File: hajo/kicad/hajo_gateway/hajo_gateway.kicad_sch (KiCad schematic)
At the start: 20 parts, among them J1 Seetalk NG, J2 WitMtoion, U1 MCP2562, U2 LF50, U3 WeMos_S2_mini, U4 LF33, U5 MAX3232

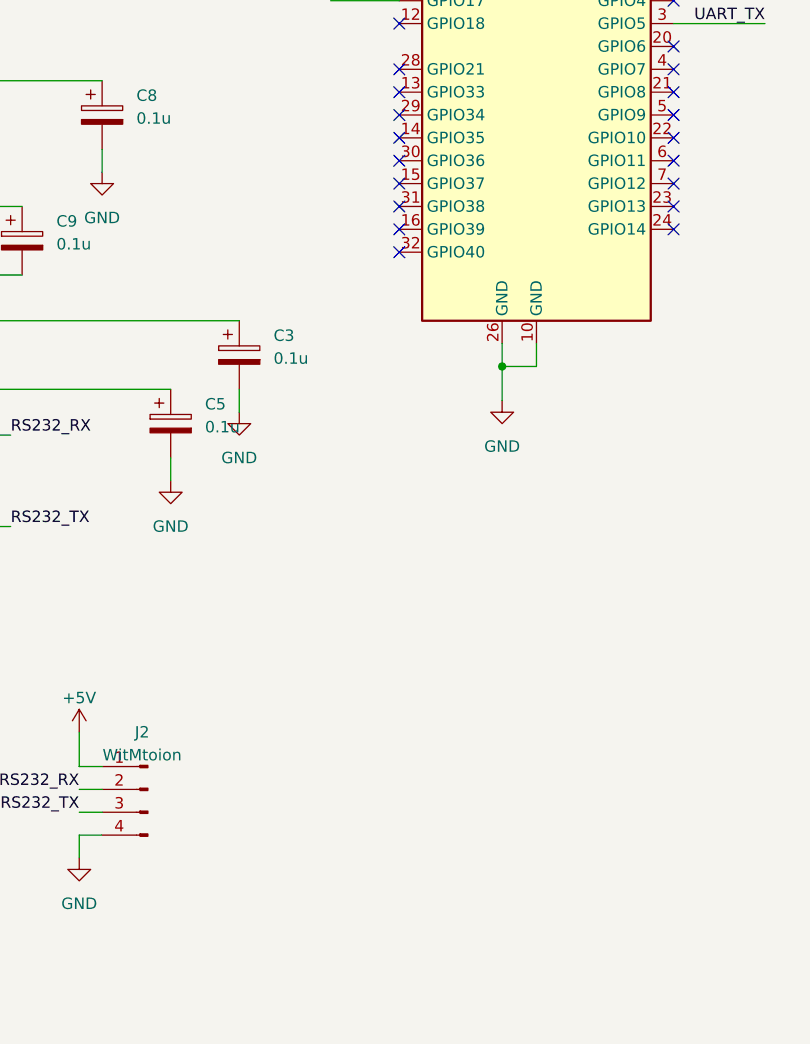
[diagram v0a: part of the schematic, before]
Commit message: add actisense header
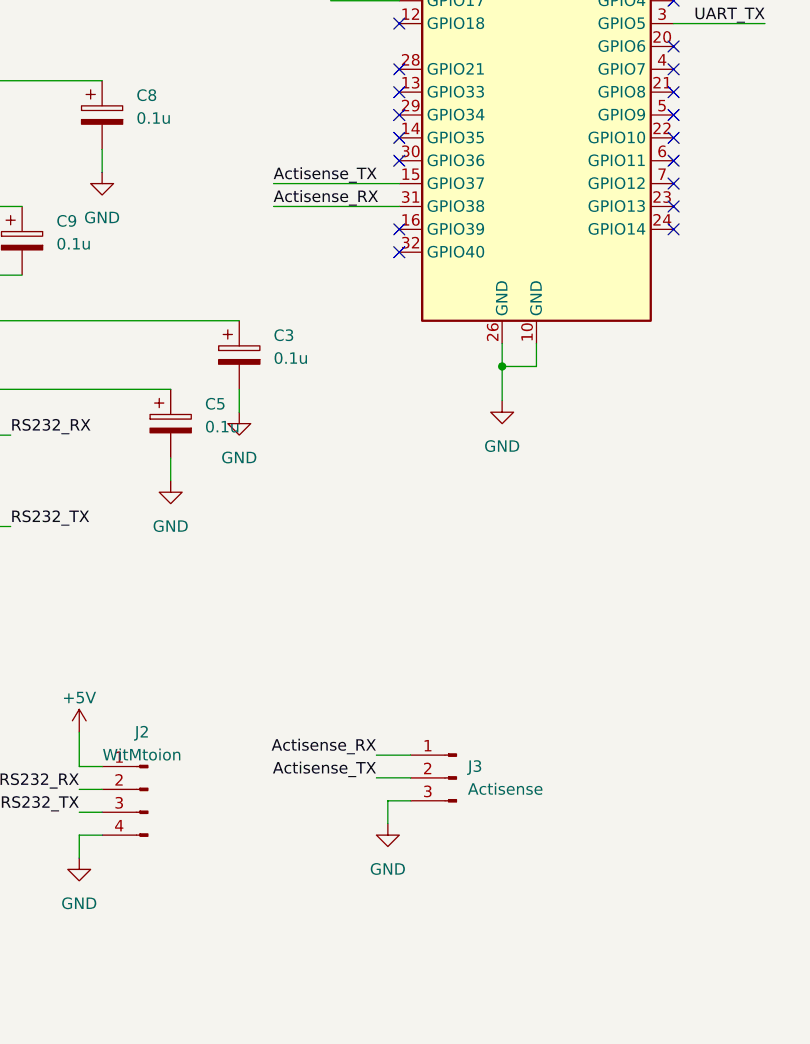
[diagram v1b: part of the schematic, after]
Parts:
- added J3: Actisense, Connector_JST:JST_XH_B3B-XH-A_1x03_P2.50mm_Vertical, symbol Connector:Conn_01x03_Pin
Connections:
- net GND: now also J3.3 (Pin_3)
- net Actisense_TX: now reaches U3.15 (GPIO37)
- net Actisense_TX: now also J3.2 (Pin_2)
- net Actisense_RX: now reaches U3.31 (GPIO38)
- net Actisense_RX: now also J3.1 (Pin_1)
- no-connect marks 27 -> 25
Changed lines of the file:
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@@
 	)
 	(no_connect
-		(at 165.1 72.39)
-	)
-	(no_connect
 		(at 165.1 54.61)
 	)
@@
 	)
 	(no_connect
-		(at 165.1 74.93)
-	)
-	(no_connect
 		(at 165.1 39.37)
 	)
@@
 	(wire
 		(pts
+			(xy 151.13 72.39) (xy 165.1 72.39)
+		)
+		(stroke
+			(width 0)
+			(type default)
+		)
+	)
+	(wire
+		(pts
 			(xy 119.38 110.49) (xy 121.92 110.49)
 		)
@@
 	(wire
 		(pts
+			(xy 162.56 138.43) (xy 166.37 138.43)
+		)
+		(stroke
+			(width 0)
+			(type default)
+		)
+	)
+	(wire
+		(pts
 			(xy 29.21 41.91) (xy 36.83 41.91)
 		)
@@
 	(wire
 		(pts
+			(xy 151.13 74.93) (xy 165.1 74.93)
+		)
+		(stroke
+			(width 0)
+			(type default)
+		)
+	)
+	(wire
+		(pts
 			(xy 195.58 44.45) (xy 203.2 44.45)
 		)
@@
 	(wire
 		(pts
+			(xy 163.83 140.97) (xy 163.83 143.51)
+		)
+		(stroke
+			(width 0)
+			(type default)
+		)
+	)
+	(wire
+		(pts
 			(xy 129.54 142.24) (xy 132.08 142.24)
 		)
@@
 	(wire
 		(pts
+			(xy 166.37 140.97) (xy 163.83 140.97)
+		)
+		(stroke
+			(width 0)
+			(type default)
+		)
+	)
+	(wire
+		(pts
 			(xy 29.21 31.75) (xy 36.83 31.75)
 		)
@@
 	(wire
 		(pts
+			(xy 162.56 135.89) (xy 166.37 135.89)
+		)
+		(stroke
+			(width 0)
+			(type default)
+		)
+	)
+	(wire
+		(pts
 			(xy 29.21 41.91) (xy 29.21 48.26)
 		)
@@
 		)
 	)
+	(label "Actisense_TX"
+		(at 162.56 138.43 180)
+		(fields_autoplaced yes)
+		(effects
+			(font
+				(size 1.27 1.27)
+			)
+			(justify right bottom)
+		)
+	)
 	(label "RS232_RX"
 		(at 129.54 139.7 180)
@@
 		)
 	)
+	(label "Actisense_TX"
+		(at 151.13 72.39 0)
+		(fields_autoplaced yes)
+		(effects
+			(font
+				(size 1.27 1.27)
+			)
+			(justify left bottom)
+		)
+	)
 	(label "DevType"
 		(at 203.2 46.99 180)
@@
 		)
 	)
+	(label "Actisense_RX"
+		(at 151.13 74.93 0)
+		(fields_autoplaced yes)
+		(effects
+			(font
+				(size 1.27 1.27)
+			)
+			(justify left bottom)
+		)
+	)
 	(label "CANH"
 		(at 66.04 34.29 0)
@@
 		)
 	)
+	(label "Actisense_RX"
+		(at 162.56 135.89 180)
+		(fields_autoplaced yes)
+		(effects
+			(font
+				(size 1.27 1.27)
+			)
+			(justify right bottom)
+		)
+	)
 	(symbol
 		(lib_id "Mechanical:MountingHole")
@@
 	(symbol
 		(lib_id "power:GND")
+		(at 163.83 143.51 0)
+		(unit 1)
+		(exclude_from_sim no)
+		(in_bom yes)
+		(on_board yes)
+		(dnp no)
+		(fields_autoplaced yes)
+		(property "Reference" "#PWR010"
+			(at 163.83 149.86 0)
+			(effects
+				(font
+					(size 1.27 1.27)
+				)
+				(hide yes)
+			)
+		)
+		(property "Value" "GND"
+			(at 163.83 148.59 0)
+			(effects
+				(font
+					(size 1.27 1.27)
+				)
+			)
+		)
+		(property "Footprint" ""
+			(at 163.83 143.51 0)
+			(effects
+				(font
+					(size 1.27 1.27)
+				)
+				(hide yes)
+			)
+		)
+		(property "Datasheet" ""
+			(at 163.83 143.51 0)
+			(effects
+				(font
+					(size 1.27 1.27)
+				)
+				(hide yes)
+			)
+		)
+		(property "Description" "Power symbol creates a global label with name \"GND\" , ground"
+			(at 163.83 143.51 0)
+			(effects
+				(font
+					(size 1.27 1.27)
+				)
+				(hide yes)
+			)
+		)
+		(pin "1"
+		)
+		(instances
+			(project "hajo_gateway"
+				(path "/900bec57-3a0d-41dc-a45c-3ae29a4b144e"
+					(reference "#PWR010")
+					(unit 1)
+				)
+			)
+		)
+	)
+	(symbol
+		(lib_id "power:GND")
 		(at 40.64 91.44 0)
 		(unit 1)
@@
 					(unit 1)
 				)
+			)
+		)
+	)
+	(symbol
+		(lib_id "Connector:Conn_01x03_Pin")
+		(at 171.45 138.43 0)
+		(mirror y)
+		(unit 1)
+		(exclude_from_sim no)
+		(in_bom yes)
+		(on_board yes)
+		(dnp no)
+		(fields_autoplaced yes)
+		(property "Reference" "J3"
+			(at 172.72 137.1599 0)
+			(effects
+				(font
+					(size 1.27 1.27)
+				)
+				(justify right)
+			)
+		)
+		(property "Value" "Actisense"
+			(at 172.72 139.6999 0)
+			(effects
+				(font
+					(size 1.27 1.27)
+				)
+				(justify right)
+			)
+		)
+		(property "Footprint" "Connector_JST:JST_XH_B3B-XH-A_1x03_P2.50mm_Vertical"
+			(at 171.45 138.43 0)
+			(effects
+				(font
+					(size 1.27 1.27)
+				)
+				(hide yes)
+			)
+		)
+		(property "Datasheet" "~"
+			(at 171.45 138.43 0)
+			(effects
+				(font
+					(size 1.27 1.27)
+				)
+				(hide yes)
+			)
+		)
+		(property "Description" "Generic connector, single row, 01x03, script generated"
+			(at 171.45 138.43 0)
+			(effects
+				(font
+					(size 1.27 1.27)
+				)
+				(hide yes)
+			)
+		)
+		(pin "1"
+		)
+		(pin "3"
+		)
+		(pin "2"
+		)
+		(instances
+			(project ""
+				(path "/900bec57-3a0d-41dc-a45c-3ae29a4b144e"
+					(reference "J3")
+					(unit 1)
+				)

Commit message: redesign gateway pcb
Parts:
- removed C2, C6: 100n, Capacitor_THT:C_Rect_L7.0mm_W2.0mm_P5.00mm, symbol Device:C
- added JP1: Actisense GND, Connector_PinHeader_2.54mm:PinHeader_1x02_P2.54mm_Vertical, symbol Jumper:Jumper_2_Open
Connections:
- net CANH: now also J1.2 (Pin_2); no longer J1.3 (Pin_3)
- net CANL: now also J1.3 (Pin_3); no longer J1.4 (Pin_4)
- net GND: now also J1.4 (Pin_4), JP1.1 (A); no longer J1.2 (Pin_2), J3.3 (Pin_3)
- new net: J3.3 (Pin_3), JP1.2 (B)

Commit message: redesign akku pcb
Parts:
- JP1: footprint Connector_PinHeader_2.54mm:PinHeader_1x02_P2.54mm_Vertical -> Connector_PinHeader_2.54mm:PinHeader_1x03_P2.54mm_Vertical
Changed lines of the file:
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@@
 			)
 		)
-		(property "Footprint" "Connector_PinHeader_2.54mm:PinHeader_1x02_P2.54mm_Vertical"
+		(property "Footprint" "Connector_PinHeader_2.54mm:PinHeader_1x03_P2.54mm_Vertical"
 			(at 163.83 148.59 0)
 			(effects

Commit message: fix pcb
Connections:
- net GND: now also C5.1; no longer C5.2
- net at U5.6 (VS-): now also C5.2; no longer C5.1
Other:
- moved on the sheet: C5
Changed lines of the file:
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@@
 	(symbol
 		(lib_id "Device:C_Polarized")
-		(at 139.7 99.06 0)
+		(at 139.7 99.06 180)
 		(unit 1)
 		(exclude_from_sim no)
@@
 		(dnp no)
 		(property "Reference" "C5"
-			(at 143.51 96.9009 0)
+			(at 135.89 101.2191 0)
 			(effects
 				(font
@@
 		)
 		(property "Value" "0.1u"
-			(at 143.51 99.4409 0)
+			(at 135.89 98.6791 0)
 			(effects
 				(font
@@
 		)
 		(property "Footprint" "Capacitor_THT:CP_Radial_D5.0mm_P2.50mm"
-			(at 140.6652 102.87 0)
+			(at 138.7348 95.25 0)
 			(effects
 				(font

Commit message: fix gateway pcb
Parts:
- added JP2: +5V from USB, Connector_PinHeader_2.54mm:PinHeader_1x02_P2.54mm_Vertical, symbol Jumper:Jumper_2_Open
- JP1: value Actisense GND -> GND
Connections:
- net +5V: now also JP2.1 (A)
- net at U3.9 (VBUS): now also JP2.2 (B)
- no-connect marks 25 -> 24
